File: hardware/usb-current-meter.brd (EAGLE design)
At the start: 28.9 x 16.2 mm, 28 parts, among them IC2 OPA2234U, U1 ATTINY45, X1 MC2, X3 USB-A-H

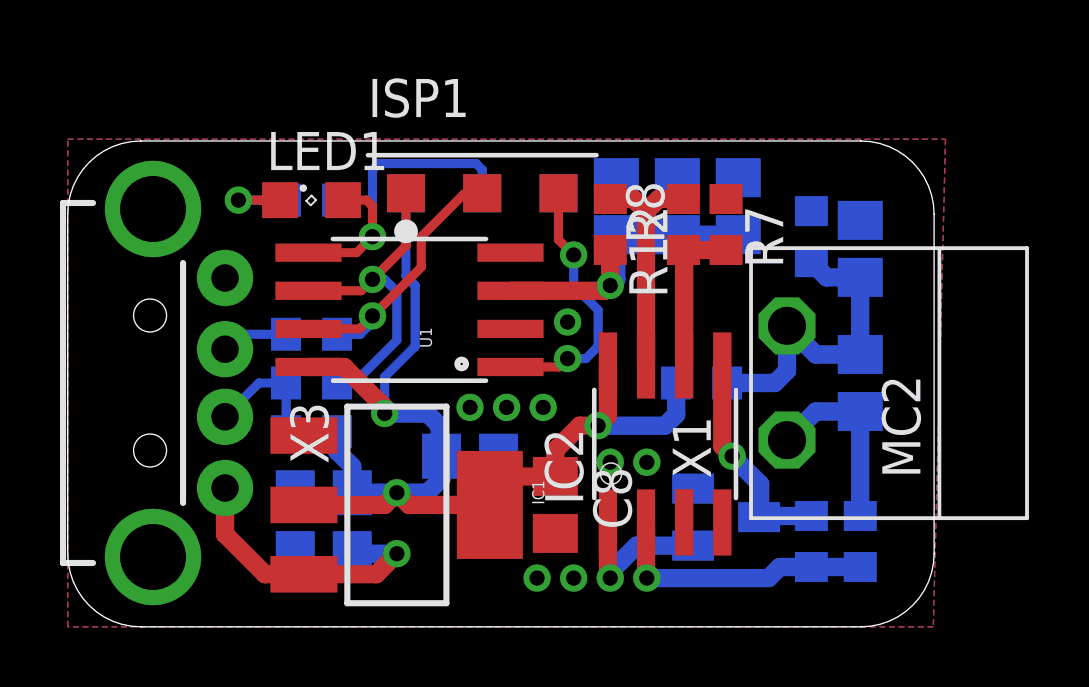
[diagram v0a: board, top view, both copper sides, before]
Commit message: hardware: add license, silkscreen
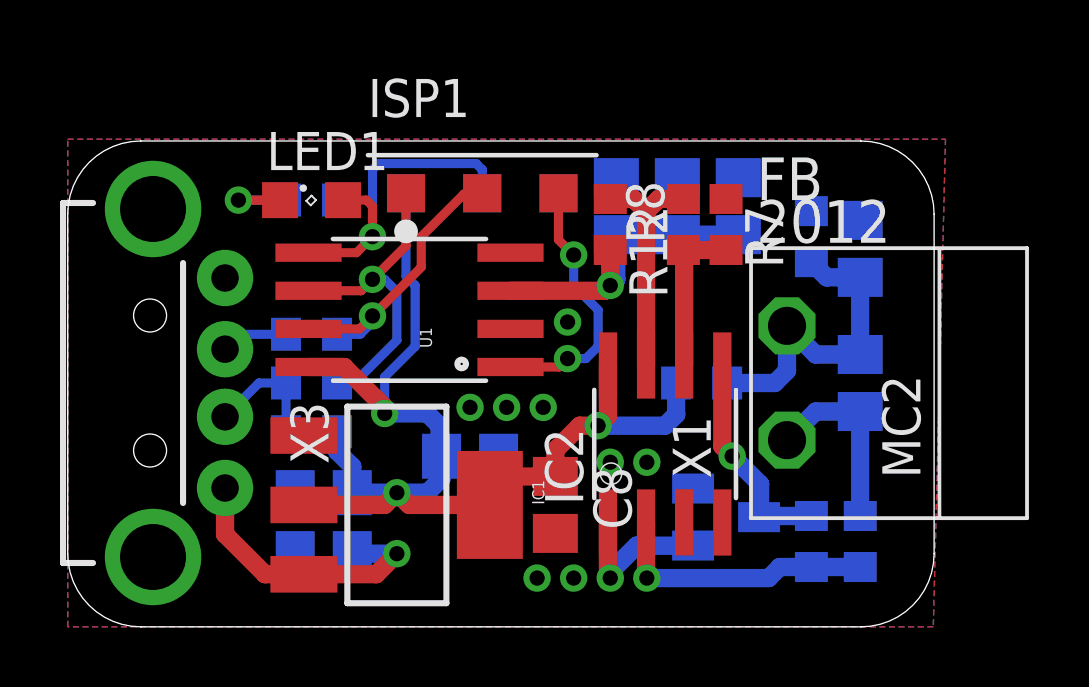
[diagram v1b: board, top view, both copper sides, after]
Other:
- board text added: "*"
- board text added: "2012"
- board text added: "FB"
- board text added: "_"
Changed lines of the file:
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@@
 <wire x1="0.4064" y1="13.7568" x2="0.4064" y2="2.4384" width="0" layer="20"/>
 <wire x1="0.4064" y1="2.4384" x2="2.8448" y2="0" width="0" layer="20" curve="90"/>
+<text x="23.368" y="14.224" size="1.4224" layer="121">FB</text>
+<text x="23.368" y="12.8016" size="1.4224" layer="121">2012</text>
+<text x="15.8496" y="13.8176" size="2.54" layer="122">_</text>
+<text x="21.336" y="8.7376" size="2.54" layer="122">*</text>
 </plain>
 <attributes>

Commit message: hardware: add some filtering capacitors
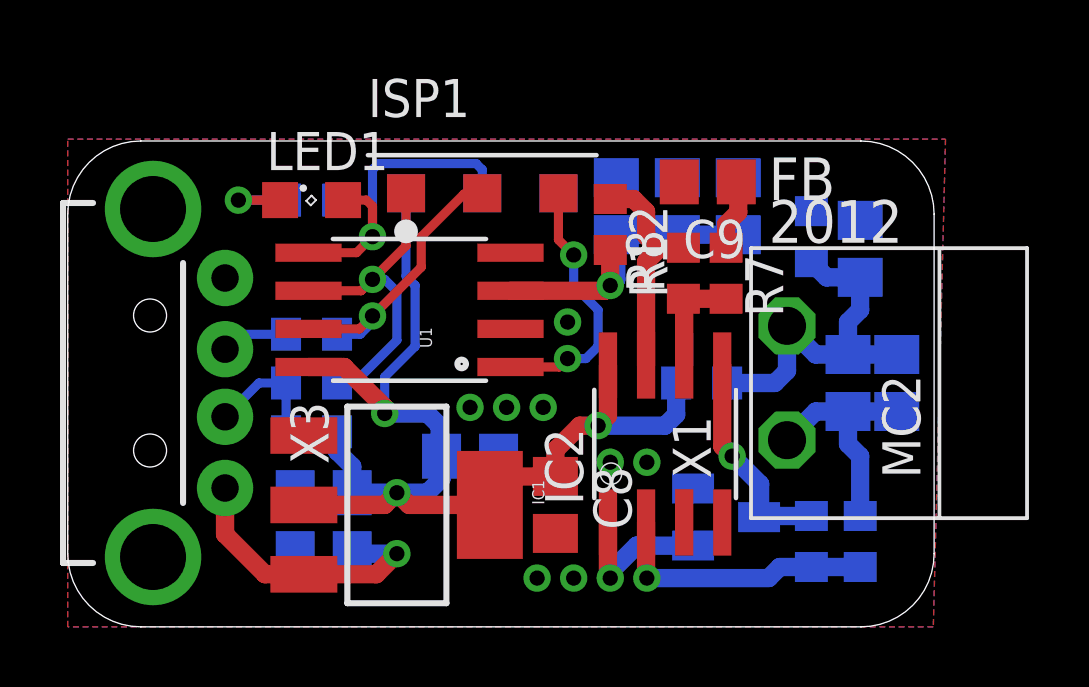
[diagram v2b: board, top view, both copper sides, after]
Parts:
- added C10: 1u, rcl:C0805
- added C9: tbd, rcl:C0805
- IC2: value OPA2234U -> LM358
- moved R7 1.63 mm to (22.4, 11.8)
- moved R8 1.63 mm to (20.9, 11.8)
- moved R4 0.41 mm to (26.4, 8.13)
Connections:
- new net N$4: C9.1, R7.1
- net GND: now also C9.2; no longer R7.1
- net SC_IN_A: now also C10.1
- net SC_IN_B: now also C10.2
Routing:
- net N$4: track 0.00 -> 2.39 mm
- net N$11: track 5.28 -> 3.66 mm
- net SC_IN_A: track 6.32 -> 7.70 mm
- net SC_IN_B: track 10.9 -> 12.3 mm
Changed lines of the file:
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@@
 <setting verticaltext="up"/>
 </settings>
-<grid distance="8" unitdist="mil" unit="mil" style="lines" multiple="1" display="no" altdistance="0.025" altunitdist="inch" altunit="inch"/>
+<grid distance="8" unitdist="mil" unit="mil" style="lines" multiple="1" display="yes" altdistance="0.025" altunitdist="inch" altunit="inch"/>
 <layers>
 <layer number="1" name="Top" color="4" fill="1" visible="yes" active="yes"/>
@@
 <wire x1="0.4064" y1="13.7568" x2="0.4064" y2="2.4384" width="0" layer="20"/>
 <wire x1="0.4064" y1="2.4384" x2="2.8448" y2="0" width="0" layer="20" curve="90"/>
-<text x="23.368" y="14.224" size="1.4224" layer="121">FB</text>
-<text x="23.368" y="12.8016" size="1.4224" layer="121">2012</text>
+<text x="23.7744" y="14.224" size="1.4224" layer="121">FB</text>
+<text x="23.7744" y="12.8016" size="1.4224" layer="121">2012</text>
 <text x="15.8496" y="13.8176" size="2.54" layer="122">_</text>
 <text x="21.336" y="8.7376" size="2.54" layer="122">*</text>
@@
 <element name="R1" library="rcl" package="R0603" value="68" x="8.5344" y="9.7536" rot="MR180"/>
 <element name="X3" library="SparkFun" package="USB-A-H" value="USB-A-H" x="3.2512" y="8.128"/>
-<element name="IC2" library="burr-brown" package="SO08" value="OPA2234U" x="20.32" y="6.096">
+<element name="IC2" library="burr-brown" package="SO08" value="LM358" x="20.32" y="6.096">
 <attribute name="OC_NEWARK" value="96K4523" x="38.1" y="-12.954" size="1.778" layer="27" display="off"/>
 <attribute name="MPN" value="OPA2234U" x="38.1" y="-12.954" size="1.778" layer="27" display="off"/>
 <attribute name="MF" value="TEXAS INSTRUMENTS" x="38.1" y="-12.954" size="1.778" layer="27" display="off"/>
 <attribute name="OC_FARNELL" value="1212441" x="38.1" y="-12.954" size="1.778" layer="27" display="off"/>
-<variant name="bias" populate="no"/>
+<variant name="bias" populate="no" value="OPA2234U"/>
 </element>
 <element name="X1" library="con-phoenix-381_l" package="MC2" value="MC2" x="24.384" y="8.128" rot="R90"/>
@@
 <element name="C2" library="rcl" package="C0805" value="100n" x="8.9408" y="2.4384" rot="MR0"/>
 <element name="C3" library="rcl" package="C0805" value="100n" x="13.8176" y="5.6896" rot="MR180"/>
-<element name="R4" library="rcl" package="R0805" value="Rload" x="26.8224" y="8.128" rot="MR270">
+<element name="R4" library="rcl" package="R0805" value="Rload" x="26.416" y="8.128" rot="MR270">
 <variant name="rectifier" populate="no"/>
 <variant name="bias" populate="no"/>
@@
 <variant name="bias" value="0"/>
 </element>
-<element name="R7" library="rcl" package="R0603" value="tbd" x="22.352" y="13.4112" rot="R270">
+<element name="R7" library="rcl" package="R0603" value="tbd" x="22.352" y="11.7856" rot="R270">
 <variant name="bias" populate="no"/>
 </element>
-<element name="R8" library="rcl" package="R0603" value="tbd" x="20.9296" y="13.4112" rot="R90">
+<element name="R8" library="rcl" package="R0603" value="tbd" x="20.9296" y="11.7856" rot="R90">
 <variant name="bias" populate="no"/>
 </element>
@@
 <variant name="bias" populate="no"/>
 </element>
+<element name="C9" library="rcl" package="C0805" value="tbd" x="21.7424" y="14.8336" rot="R180"/>
+<element name="C10" library="rcl" package="C0805" value="1u" x="28.0416" y="8.128" rot="MR90"/>
 </elements>
 <signals>
@@
 <contactref element="IC2" pad="4"/>
 <contactref element="IC2" pad="3"/>
-<contactref element="R7" pad="1"/>
 <contactref element="C5" pad="2"/>
 <contactref element="R11" pad="1"/>
@@
 <via x="13.8176" y="7.3152" extent="1-16" drill="0.508"/>
 <via x="17.0688" y="10.16" extent="1-16" drill="0.508"/>
+<contactref element="C9" pad="2"/>
 </signal>
 <signal name="N$1">
@@
 <contactref element="IC2" pad="6"/>
 <contactref element="R8" pad="1"/>
-<wire x1="22.352" y1="12.5612" x2="20.9296" y2="12.5612" width="0.6096" layer="1"/>
-<wire x1="20.955" y1="8.7122" x2="20.955" y2="12.5358" width="0.6096" layer="1"/>
-<wire x1="20.955" y1="12.5358" x2="20.9296" y2="12.5612" width="0.6096" layer="1"/>
+<wire x1="22.352" y1="10.9356" x2="20.9296" y2="10.9356" width="0.6096" layer="1"/>
+<wire x1="20.955" y1="8.7122" x2="20.955" y2="10.9102" width="0.6096" layer="1"/>
+<wire x1="20.955" y1="10.9102" x2="20.9296" y2="10.9356" width="0.6096" layer="1"/>
 </signal>
 <signal name="N$12">
@@
 <contactref element="R8" pad="2"/>
 <contactref element="R12" pad="1"/>
-<wire x1="19.685" y1="8.7122" x2="19.685" y2="13.843" width="0.6096" layer="1"/>
+<wire x1="18.4912" y1="14.2612" x2="19.2668" y2="14.2612" width="0.6096" layer="1"/>
+<wire x1="20.9296" y1="12.621096875" x2="20.9296" y2="12.6356" width="0.6096" layer="1"/>
 <wire x1="19.685" y1="13.843" x2="19.2668" y2="14.2612" width="0.6096" layer="1"/>
-<wire x1="18.4912" y1="14.2612" x2="19.2668" y2="14.2612" width="0.6096" layer="1"/>
-<wire x1="20.9296" y1="14.2612" x2="20.1032" y2="14.2612" width="0.6096" layer="1"/>
-<wire x1="20.1032" y1="14.2612" x2="19.685" y2="13.843" width="0.6096" layer="1"/>
+<wire x1="19.685" y1="8.7122" x2="19.685" y2="12.1666" width="0.6096" layer="1"/>
+<wire x1="19.685" y1="12.1666" x2="20.1168" y2="12.5984" width="0.6096" layer="1"/>
+<wire x1="19.685" y1="13.843" x2="19.685" y2="13.0302" width="0.6096" layer="1"/>
+<wire x1="19.685" y1="13.0302" x2="20.1168" y2="12.5984" width="0.6096" layer="1"/>
+<wire x1="20.1168" y1="12.5984" x2="20.8924" y2="12.5984" width="0.6096" layer="1"/>
+<wire x1="20.8924" y1="12.5984" x2="20.9296" y2="12.6356" width="0.6096" layer="1"/>
 </signal>
 <signal name="SC_IN_A">
@@
 <contactref element="X1" pad="1"/>
 <contactref element="R4" pad="2"/>
-<wire x1="26.8224" y1="7.178" x2="25.339" y2="7.178" width="0.6096" layer="16"/>
+<wire x1="26.416" y1="7.178" x2="25.339" y2="7.178" width="0.6096" layer="16"/>
 <wire x1="25.339" y1="7.178" x2="24.384" y2="6.223" width="0.6096" layer="16"/>
-<wire x1="26.8224" y1="7.178" x2="26.8224" y2="3.6948" width="0.6096" layer="16"/>
+<contactref element="C10" pad="1"/>
+<wire x1="26.8224" y1="3.6948" x2="26.8224" y2="5.6896" width="0.6096" layer="16"/>
+<wire x1="26.8224" y1="5.6896" x2="26.416" y2="6.096" width="0.6096" layer="16"/>
+<wire x1="26.416" y1="6.096" x2="26.416" y2="7.178" width="0.6096" layer="16"/>
+<wire x1="26.416" y1="7.178" x2="28.0416" y2="7.178" width="0.6096" layer="16"/>
 </signal>
 <signal name="SC_IN_B">
@@
 <contactref element="R11" pad="2"/>
 <contactref element="C5" pad="1"/>
-<wire x1="26.8224" y1="9.078" x2="25.339" y2="9.078" width="0.6096" layer="16"/>
+<wire x1="26.416" y1="9.078" x2="25.339" y2="9.078" width="0.6096" layer="16"/>
 <wire x1="25.339" y1="9.078" x2="24.384" y2="10.033" width="0.6096" layer="16"/>
 <wire x1="26.8224" y1="11.6484" x2="25.7032" y2="11.6484" width="0.6096" layer="16"/>
 <wire x1="25.7032" y1="11.6484" x2="25.1968" y2="12.1548" width="0.6096" layer="16"/>
-<wire x1="26.8224" y1="11.6484" x2="26.8224" y2="9.078" width="0.6096" layer="16"/>
 <wire x1="22.3892" y1="8.128" x2="23.9776" y2="8.128" width="0.6096" layer="16"/>
 <wire x1="23.9776" y1="8.128" x2="24.384" y2="8.5344" width="0.6096" layer="16"/>
 <wire x1="24.384" y1="8.5344" x2="24.384" y2="10.033" width="0.6096" layer="16"/>
+<contactref element="C10" pad="2"/>
+<wire x1="26.8224" y1="11.6484" x2="26.8224" y2="10.5664" width="0.6096" layer="16"/>
+<wire x1="26.8224" y1="10.5664" x2="26.416" y2="10.16" width="0.6096" layer="16"/>
+<wire x1="26.416" y1="10.16" x2="26.416" y2="9.078" width="0.6096" layer="16"/>
+<wire x1="26.416" y1="9.078" x2="28.0416" y2="9.078" width="0.6096" layer="16"/>
 </signal>
 <signal name="SC_OUT">
@@
 <wire x1="17.6784" y1="8.9408" x2="17.0688" y2="8.9408" width="0.3048" layer="16"/>
 </signal>
+<signal name="N$4">
+<contactref element="C9" pad="1"/>
+<contactref element="R7" pad="1"/>
+<wire x1="22.352" y1="12.6356" x2="22.352" y2="13.4112" width="0.6096" layer="1"/>
+<wire x1="22.352" y1="13.4112" x2="22.7584" y2="13.8176" width="0.6096" layer="1"/>
+<wire x1="22.7584" y1="13.8176" x2="22.7584" y2="14.7676" width="0.6096" layer="1"/>
+<wire x1="22.7584" y1="14.7676" x2="22.6924" y2="14.8336" width="0.6096" layer="1"/>
+</signal>
 </signals>
+<errors>
+</errors>
 </board>
 </drawing>

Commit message: hw: change opamp to lt2078
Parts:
- IC2: value LM358 -> LT2078
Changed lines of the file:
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@@
 <?xml version="1.0" encoding="utf-8"?>
 <!DOCTYPE eagle SYSTEM "eagle.dtd">
-<eagle version="6.1">
+<eagle version="6.2">
 <drawing>
 <settings>
@@
 <element name="R1" library="rcl" package="R0603" value="68" x="8.5344" y="9.7536" rot="MR180"/>
 <element name="X3" library="SparkFun" package="USB-A-H" value="USB-A-H" x="3.2512" y="8.128"/>
-<element name="IC2" library="burr-brown" package="SO08" value="LM358" x="20.32" y="6.096">
+<element name="IC2" library="burr-brown" package="SO08" value="LT2078" x="20.32" y="6.096">
 <attribute name="OC_NEWARK" value="96K4523" x="38.1" y="-12.954" size="1.778" layer="27" display="off"/>
 <attribute name="MPN" value="OPA2234U" x="38.1" y="-12.954" size="1.778" layer="27" display="off"/>
